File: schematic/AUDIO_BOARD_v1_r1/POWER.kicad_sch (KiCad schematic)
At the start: 18 parts, among them J1 PWR FFC 4p, U1 LTC660, U15 LTC660

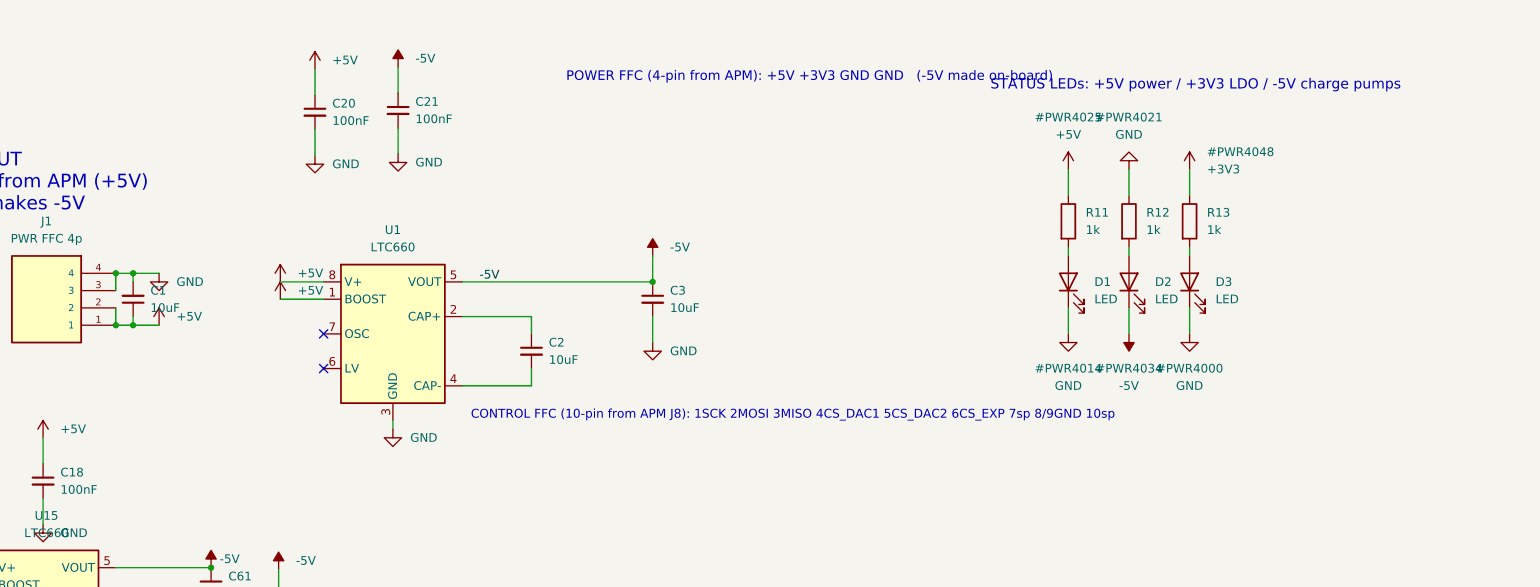
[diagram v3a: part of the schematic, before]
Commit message: U2B not connected
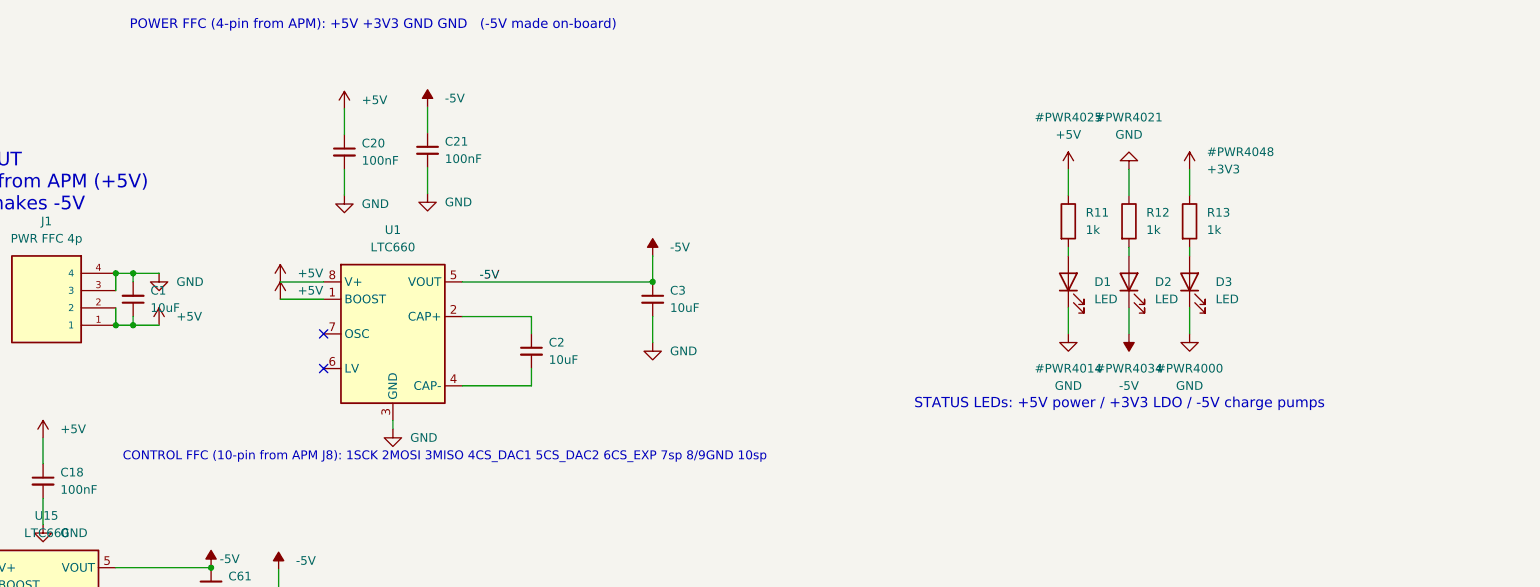
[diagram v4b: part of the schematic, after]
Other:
- moved on the sheet: C20, C21
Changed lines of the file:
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@@
 	(text "POWER FFC (4-pin from APM): +5V +3V3 GND GND   (-5V made on-board)"
 		(exclude_from_sim no)
-		(at 207.518 41.91 0)
+		(at 143.51 34.29 0)
 		(effects
 			(font
@@
 	(text "CONTROL FFC (10-pin from APM J8): 1SCK 2MOSI 3MISO 4CS_DAC1 5CS_DAC2 6CS_EXP 7sp 8/9GND 10sp"
 		(exclude_from_sim no)
-		(at 193.548 91.44 0)
+		(at 142.494 97.536 0)
 		(effects
 			(font
@@
 	(text "STATUS LEDs: +5V power / +3V3 LDO / -5V charge pumps"
 		(exclude_from_sim no)
-		(at 269.748 43.18 0)
+		(at 258.572 89.916 0)
 		(effects
 			(font
@@
 	(wire
 		(pts
-			(xy 170.688 43.688) (xy 170.688 39.878)
+			(xy 175.006 49.53) (xy 175.006 45.72)
 		)
 		(stroke
@@
 	(wire
 		(pts
-			(xy 182.88 48.514) (xy 182.88 52.324)
+			(xy 187.198 54.356) (xy 187.198 58.166)
 		)
 		(stroke
@@
 	(wire
 		(pts
-			(xy 182.88 43.434) (xy 182.88 39.624)
+			(xy 187.198 49.276) (xy 187.198 45.466)
 		)
 		(stroke
@@
 	(wire
 		(pts
-			(xy 170.688 48.768) (xy 170.688 52.578)
+			(xy 175.006 54.61) (xy 175.006 58.42)
 		)
 		(stroke
@@
 	(symbol
 		(lib_id "Device:C_Small")
-		(at 182.88 45.974 0)
+		(at 187.198 51.816 0)
 		(unit 1)
 		(body_style 1)
@@
 		(fields_autoplaced yes)
 		(property "Reference" "C21"
-			(at 185.42 44.704 0)
+			(at 189.738 50.546 0)
 			(show_name no)
 			(do_not_autoplace no)
@@
 		)
 		(property "Value" "100nF"
-			(at 185.42 47.244 0)
+			(at 189.738 53.086 0)
 			(show_name no)
 			(do_not_autoplace no)
@@
 		)
 		(property "Footprint" "Capacitor_SMD:C_0402_1005Metric"
-			(at 182.88 45.974 0)
+			(at 187.198 51.816 0)
 			(hide yes)
 			(show_name no)
@@
 		)
 		(property "Datasheet" ""
-			(at 182.88 45.974 0)
+			(at 187.198 51.816 0)
 			(show_name no)
 			(do_not_autoplace no)
@@
 		)
 		(property "Description" ""
-			(at 182.88 45.974 0)
+			(at 187.198 51.816 0)
 			(show_name no)
 			(do_not_autoplace no)
@@
 	(symbol
 		(lib_id "power:-5V")
-		(at 182.88 39.624 0)
+		(at 187.198 45.466 0)
 		(unit 1)
 		(body_style 1)
@@
 		(fields_autoplaced yes)
 		(property "Reference" "#PWR4002"
-			(at 182.88 42.164 0)
+			(at 187.198 48.006 0)
 			(hide yes)
 			(show_name no)
@@
 		)
 		(property "Value" "-5V"
-			(at 185.42 38.354 0)
+			(at 189.738 44.196 0)
 			(show_name no)
 			(do_not_autoplace no)
@@
 		)
 		(property "Footprint" ""
-			(at 182.88 39.624 0)
+			(at 187.198 45.466 0)
 			(show_name no)
 			(do_not_autoplace no)
@@
 		)
 		(property "Datasheet" ""
-			(at 182.88 39.624 0)
+			(at 187.198 45.466 0)
 			(show_name no)
 			(do_not_autoplace no)
@@
 		)
 		(property "Description" ""
-			(at 182.88 39.624 0)
+			(at 187.198 45.466 0)
 			(show_name no)
 			(do_not_autoplace no)
@@
 	(symbol
 		(lib_id "power:+5V")
-		(at 170.688 39.878 0)
+		(at 175.006 45.72 0)
 		(unit 1)
 		(body_style 1)
@@
 		(fields_autoplaced yes)
 		(property "Reference" "#PWR4008"
-			(at 170.688 42.418 0)
+			(at 175.006 48.26 0)
 			(hide yes)
 			(show_name no)
@@
 		)
 		(property "Value" "+5V"
-			(at 173.228 38.608 0)
+			(at 177.546 44.45 0)
 			(show_name no)
 			(do_not_autoplace no)
@@
 		)
 		(property "Footprint" ""
-			(at 170.688 39.878 0)
+			(at 175.006 45.72 0)
 			(show_name no)
 			(do_not_autoplace no)
@@
 		)
 		(property "Datasheet" ""
-			(at 170.688 39.878 0)
+			(at 175.006 45.72 0)
 			(show_name no)
 			(do_not_autoplace no)
@@
 		)
 		(property "Description" ""
-			(at 170.688 39.878 0)
+			(at 175.006 45.72 0)
 			(show_name no)
 			(do_not_autoplace no)
@@
 	(symbol
 		(lib_id "Device:C_Small")
-		(at 170.688 46.228 0)
+		(at 175.006 52.07 0)
 		(unit 1)
 		(body_style 1)
@@
 		(fields_autoplaced yes)
 		(property "Reference" "C20"
-			(at 173.228 44.958 0)
+			(at 177.546 50.8 0)
 			(show_name no)
 			(do_not_autoplace no)
@@
 		)
 		(property "Value" "100nF"
-			(at 173.228 47.498 0)
+			(at 177.546 53.34 0)
 			(show_name no)
 			(do_not_autoplace no)
@@
 		)
 		(property "Footprint" "Capacitor_SMD:C_0402_1005Metric"
-			(at 170.688 46.228 0)
+			(at 175.006 52.07 0)
 			(hide yes)
 			(show_name no)
@@
 		)
 		(property "Datasheet" ""
-			(at 170.688 46.228 0)
+			(at 175.006 52.07 0)
 			(show_name no)
 			(do_not_autoplace no)
@@
 		)
 		(property "Description" ""
-			(at 170.688 46.228 0)
+			(at 175.006 52.07 0)
 			(show_name no)
 			(do_not_autoplace no)
@@
 	(symbol
 		(lib_id "power:GND")
-		(at 170.688 52.578 0)
+		(at 175.006 58.42 0)
 		(unit 1)
 		(body_style 1)
@@
 		(fields_autoplaced yes)
 		(property "Reference" "#PWR4032"
-			(at 170.688 55.118 0)
+			(at 175.006 60.96 0)
 			(hide yes)
 			(show_name no)
@@
 		)
 		(property "Value" "GND"
-			(at 173.228 53.848 0)
+			(at 177.546 59.69 0)
 			(show_name no)
 			(do_not_autoplace no)
@@
 		)
 		(property "Footprint" ""
-			(at 170.688 52.578 0)
+			(at 175.006 58.42 0)
 			(show_name no)
 			(do_not_autoplace no)
@@
 		)
 		(property "Datasheet" ""
-			(at 170.688 52.578 0)
+			(at 175.006 58.42 0)
 			(show_name no)
 			(do_not_autoplace no)
@@
 		)
 		(property "Description" ""
-			(at 170.688 52.578 0)
+			(at 175.006 58.42 0)
 			(show_name no)
 			(do_not_autoplace no)
@@
 	(symbol
 		(lib_id "power:GND")
-		(at 182.88 52.324 0)
+		(at 187.198 58.166 0)
 		(unit 1)
 		(body_style 1)
@@
 		(fields_autoplaced yes)
 		(property "Reference" "#PWR4042"
-			(at 182.88 54.864 0)
+			(at 187.198 60.706 0)
 			(hide yes)
 			(show_name no)
@@
 		)
 		(property "Value" "GND"
-			(at 185.42 53.594 0)
+			(at 189.738 59.436 0)
 			(show_name no)
 			(do_not_autoplace no)
@@
 		)
 		(property "Footprint" ""
-			(at 182.88 52.324 0)
+			(at 187.198 58.166 0)
 			(show_name no)
 			(do_not_autoplace no)
@@
 		)
 		(property "Datasheet" ""
-			(at 182.88 52.324 0)
+			(at 187.198 58.166 0)
 			(show_name no)
 			(do_not_autoplace no)
@@
 		)
 		(property "Description" ""
-			(at 182.88 52.324 0)
+			(at 187.198 58.166 0)
 			(show_name no)
 			(do_not_autoplace no)

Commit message: more routing. more placement
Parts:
- added C51: 100nF, Capacitor_SMD:C_0402_1005Metric, symbol Device:C_Small
- added C56, C57: 1uF, Capacitor_SMD:C_0402_1005Metric, symbol Device:C_Small
- added U22: AP2112K-3.3, Package_TO_SOT_SMD:SOT-23-5, symbol Regulator_Linear:AP2112K-3.3
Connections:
- net +3V3: now also C57.1, U22.5 (VOUT)
- net +5V: now also C51.1, C56.1, U22.1 (VIN), U22.3 (EN)
- net GND: now also C51.2, C56.2, C57.2, U22.2 (GND)
- no-connect marks 4 -> 5
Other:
- note added: "+3V3 LDO - AP2112K-3.3 from +5V (power FFC carries no +3V3); supplies only the MCP expander."
